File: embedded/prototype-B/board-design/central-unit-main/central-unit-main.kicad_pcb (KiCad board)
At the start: 2 copper layers, 0 parts

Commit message: [Central unit] PCB design
Finalized PCB design for the central unit.

Signed-off-by: Nicolae-Andrei Prodan <vasilenicolaeandrei@gmail.com>
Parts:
- added BAT1: 1043, 1043:1043, B.Cu at (142.0, 53.4)
- added C1: 100nF/6.3V/20%/C0603, Capacitor_SMD:C_0603_1608Metric_Pad1.08x0.95mm_HandSolder, F.Cu at (141.0, 105.0)
- added C10: 10pF/6.3V/20%/C0603, Capacitor_SMD:C_0603_1608Metric_Pad1.08x0.95mm_HandSolder, F.Cu at (159.0, 87.5)
- added C11: 22nF/6.3V/20%/C0603, Capacitor_SMD:C_0603_1608Metric_Pad1.08x0.95mm_HandSolder, F.Cu at (141.0, 103.0)
- added C12: 100nF/6.3V/20%/C0603, Capacitor_SMD:C_0603_1608Metric_Pad1.08x0.95mm_HandSolder, F.Cu at (147.2, 90.0)
- added C13: 100nF/6.3V/20%/C0603, Capacitor_SMD:C_0603_1608Metric_Pad1.08x0.95mm_HandSolder, F.Cu at (134.0, 95.0)
- added C14: 100nF/6.3V/20%/C0603, Capacitor_SMD:C_0603_1608Metric_Pad1.08x0.95mm_HandSolder, F.Cu at (134.0, 97.0)
- added C15: 100nF/6.3V/20%/C0603, Capacitor_SMD:C_0603_1608Metric_Pad1.08x0.95mm_HandSolder, F.Cu at (131.5, 102.0)
- added C16: 100nF/6.3V/20%/C0603, Capacitor_SMD:C_0603_1608Metric_Pad1.08x0.95mm_HandSolder, F.Cu at (133.5, 102.0)
- added C17: 2.2pF/6.3V/20%/C0603, Capacitor_SMD:C_0603_1608Metric_Pad1.08x0.95mm_HandSolder, F.Cu at (136.0, 79.5)
- added C18: 22uF/6.3V/20%/C0603, Capacitor_SMD:C_0603_1608Metric_Pad1.08x0.95mm_HandSolder, F.Cu at (142.0, 79.5)
- added C19: 10uF/6.3V/20%/C0603, Capacitor_SMD:C_0603_1608Metric_Pad1.08x0.95mm_HandSolder, F.Cu at (140.0, 79.5)
- added C2: 1uF/6.3V/20%/C0603, Capacitor_SMD:C_0603_1608Metric_Pad1.08x0.95mm_HandSolder, F.Cu at (141.0, 107.0)
- added C20: 100nF/6.3V/20%/C0603, Capacitor_SMD:C_0603_1608Metric_Pad1.08x0.95mm_HandSolder, F.Cu at (145.0, 80.5)
- added C21: 10uF/6.3V/20%/C0603, Capacitor_SMD:C_0603_1608Metric_Pad1.08x0.95mm_HandSolder, F.Cu at (138.0, 72.5)
- added C22: 100nF/6.3V/20%/C0603, Capacitor_SMD:C_0603_1608Metric_Pad1.08x0.95mm_HandSolder, F.Cu at (134.0, 76.5)
- added C23: 10uF/6.3V/20%/C0603, Capacitor_SMD:C_0603_1608Metric_Pad1.08x0.95mm_HandSolder, F.Cu at (145.5, 67.0)
- added C24: 10uF/6.3V/20%/C0603, Capacitor_SMD:C_0603_1608Metric_Pad1.08x0.95mm_HandSolder, F.Cu at (142.0, 62.0)
- added C25: 10uF/6.3V/20%/C0603, Capacitor_SMD:C_0603_1608Metric_Pad1.08x0.95mm_HandSolder, F.Cu at (138.0, 53.5)
- added C26: 10uF/6.3V/20%/C0603, Capacitor_SMD:C_0603_1608Metric_Pad1.08x0.95mm_HandSolder, F.Cu at (137.0, 63.0)
- added C27: 100nF/6.3V/20%/C0603, Capacitor_SMD:C_0603_1608Metric_Pad1.08x0.95mm_HandSolder, F.Cu at (145.0, 116.5)
- added C28: 10uF/6.3V/20%/C0603, Capacitor_SMD:C_0603_1608Metric_Pad1.08x0.95mm_HandSolder, F.Cu at (147.0, 116.5)
- added C29: 100nF/6.3V/20%/C0603, Capacitor_SMD:C_0603_1608Metric_Pad1.08x0.95mm_HandSolder, F.Cu at (146.0, 119.5)
- added C3: 1uF/6.3V/20%/C0603, Capacitor_SMD:C_0603_1608Metric_Pad1.08x0.95mm_HandSolder, F.Cu at (141.0, 93.0)
- added C30: 100nF/6.3V/20%/C0603, Capacitor_SMD:C_0603_1608Metric_Pad1.08x0.95mm_HandSolder, F.Cu at (146.0, 121.5)
- added C31: 10uF/6.3V/20%/C0603, Capacitor_SMD:C_0603_1608Metric_Pad1.08x0.95mm_HandSolder, F.Cu at (146.0, 123.5)
- added C32: 10uF/6.3V/20%/C0603, Capacitor_SMD:C_0603_1608Metric_Pad1.08x0.95mm_HandSolder, F.Cu at (125.0, 94.0)
- added C4: 10uF/6.3V/20%/C0603, Capacitor_SMD:C_0603_1608Metric_Pad1.08x0.95mm_HandSolder, F.Cu at (141.0, 89.0)
- added C5: 100nF/6.3V/20%/C0603, Capacitor_SMD:C_0603_1608Metric_Pad1.08x0.95mm_HandSolder, F.Cu at (147.5, 109.0)
- added C6: 100nF/6.3V/20%/C0603, Capacitor_SMD:C_0603_1608Metric_Pad1.08x0.95mm_HandSolder, F.Cu at (154.0, 109.0)
- added C7: 100nF/6.3V/20%/C0603, Capacitor_SMD:C_0603_1608Metric_Pad1.08x0.95mm_HandSolder, F.Cu at (141.0, 91.0)
- added C8: 100nF/6.3V/20%/C0603, Capacitor_SMD:C_0603_1608Metric_Pad1.08x0.95mm_HandSolder, F.Cu at (159.0, 96.0)
- added C9: 1uF/6.3V/20%/C0603, Capacitor_SMD:C_0603_1608Metric_Pad1.08x0.95mm_HandSolder, F.Cu at (159.0, 94.0)
- added D1: ESDA7P60-1U1M, ESDA7P60-1U1M:TVS_ESDA7P60-1U1M, F.Cu at (145.5, 65.0)
- added D3: LED, LED_SMD:LED_0805_2012Metric_Pad1.15x1.40mm_HandSolder, F.Cu at (135.0, 63.0)
- added D4: LED, LED_SMD:LED_0805_2012Metric_Pad1.15x1.40mm_HandSolder, F.Cu at (132.5, 63.0)
- added FB3: BLM18PG121SN1D, Inductor_SMD:L_0603_1608Metric_Pad1.05x0.95mm_HandSolder, F.Cu at (146.0, 125.5)
- added FB4: BLM18PG121SN1D, Inductor_SMD:L_0603_1608Metric_Pad1.05x0.95mm_HandSolder, F.Cu at (141.0, 109.0)
- added H1: MountingHole_Pad, MountingHole:MountingHole_4.3mm_M4_ISO7380_Pad, F.Cu at (125.0, 54.0)
- added H2: MountingHole_Pad, MountingHole:MountingHole_4.3mm_M4_ISO7380_Pad, F.Cu at (159.0, 54.0)
- added H3: MountingHole_Pad, MountingHole:MountingHole_4.3mm_M4_ISO7380_Pad, F.Cu at (159.0, 135.5)
- added H4: MountingHole_Pad, MountingHole:MountingHole_4.3mm_M4_ISO7380_Pad, F.Cu at (125.0, 135.5)
- added IC2: VEML6030, VEML6030:VEML6030, F.Cu at (142.0, 116.5)
- added IC3: STM1061N27WX6F, STM1061N27WX6F:SOT103P237X112-3N, F.Cu at (145.0, 75.5)
- added J1: Screw_Terminal_01x02, TerminalBlock_Phoenix:TerminalBlock_Phoenix_MPT-0,5-2-2.54_1x02_P2.54mm_Horizontal, B.Cu at (157.5, 80.0)
- added J2: 2171790001, 2171790001:MOLEX_2171790001, F.Cu at (160.5, 68.0)
- added J3: Conn_02x05_Odd_Even, Connector_IDC:IDC-Header_2x05_P2.54mm_Vertical, B.Cu at (147.1, 135.8)
- added J4: Conn_02x05_Odd_Even, Connector_IDC:IDC-Header_2x05_P2.54mm_Vertical, B.Cu at (158.0, 123.5)
- added J5: Conn_ARM_JTAG_SWD_20, Connector_IDC:IDC-Header_2x10_P2.54mm_Vertical, B.Cu at (126.0, 100.6)
- added L1: 2.2uH(MAMK2520T2R2M), Inductor_SMD:L_1008_2520Metric_Pad1.43x2.20mm_HandSolder, F.Cu at (141.5, 75.5)
- added R1: 0R/R0603, Resistor_SMD:R_0603_1608Metric_Pad0.98x0.95mm_HandSolder, F.Cu at (137.5, 99.0)
- added R10: 1M/R0603, Resistor_SMD:R_0603_1608Metric_Pad0.98x0.95mm_HandSolder, F.Cu at (134.0, 79.5)
- added R11: 178K/R0603, Resistor_SMD:R_0603_1608Metric_Pad0.98x0.95mm_HandSolder, F.Cu at (132.0, 79.5)
- added R12: 33K/R0603, Resistor_SMD:R_0603_1608Metric_Pad0.98x0.95mm_HandSolder, F.Cu at (145.5, 69.0)
- added R13: 5.1K/R0603, Resistor_SMD:R_0603_1608Metric_Pad0.98x0.95mm_HandSolder, F.Cu at (153.5, 69.5)
- added R14: 5.1K/R0603, Resistor_SMD:R_0603_1608Metric_Pad0.98x0.95mm_HandSolder, F.Cu at (153.5, 66.5)
- added R15: 82K/R0603, Resistor_SMD:R_0603_1608Metric_Pad0.98x0.95mm_HandSolder, F.Cu at (145.5, 71.0)
- added R16: 4.12K/R0603, Resistor_SMD:R_0603_1608Metric_Pad0.98x0.95mm_HandSolder, F.Cu at (142.0, 58.0)
- added R17: 46.4K/R0603, Resistor_SMD:R_0603_1608Metric_Pad0.98x0.95mm_HandSolder, F.Cu at (142.0, 60.0)
- added R18: 1.18K/R0603, Resistor_SMD:R_0603_1608Metric_Pad0.98x0.95mm_HandSolder, F.Cu at (139.0, 63.0)
- added R19: 1.13K/R0603, Resistor_SMD:R_0603_1608Metric_Pad0.98x0.95mm_HandSolder, F.Cu at (142.0, 56.0)
- added R2: 0R/R0603, Resistor_SMD:R_0603_1608Metric_Pad0.98x0.95mm_HandSolder, F.Cu at (137.5, 101.0)
- added R20: 1.5K/R0603, Resistor_SMD:R_0603_1608Metric_Pad0.98x0.95mm_HandSolder, F.Cu at (135.0, 67.0)
- added R21: 1.5K/R0603, Resistor_SMD:R_0603_1608Metric_Pad0.98x0.95mm_HandSolder, F.Cu at (132.5, 67.0)
- added R22: 10K/R0603, Resistor_SMD:R_0603_1608Metric_Pad0.98x0.95mm_HandSolder, F.Cu at (139.0, 116.5)
- added R23: 10K/R0603, Resistor_SMD:R_0603_1608Metric_Pad0.98x0.95mm_HandSolder, F.Cu at (139.0, 121.0)
- added R24: 10K/R0603, Resistor_SMD:R_0603_1608Metric_Pad0.98x0.95mm_HandSolder, F.Cu at (149.2, 90.0)
- added R25: 10K/R0603, Resistor_SMD:R_0603_1608Metric_Pad0.98x0.95mm_HandSolder, F.Cu at (151.2, 90.0)
- added R26: 10K/R0603, Resistor_SMD:R_0603_1608Metric_Pad0.98x0.95mm_HandSolder, F.Cu at (125.0, 92.0)
- added R27: 10K/R0603, Resistor_SMD:R_0603_1608Metric_Pad0.98x0.95mm_HandSolder, F.Cu at (132.5, 112.0)
- added R28: 10K/R0603, Resistor_SMD:R_0603_1608Metric_Pad0.98x0.95mm_HandSolder, F.Cu at (124.9, 88.0)
- added R29: 10K/R0603, Resistor_SMD:R_0603_1608Metric_Pad0.98x0.95mm_HandSolder, F.Cu at (125.0, 90.0)
- added R3: 0R/R0603, Resistor_SMD:R_0603_1608Metric_Pad0.98x0.95mm_HandSolder, F.Cu at (159.0, 100.0)
- added R30: 10K/R0603, Resistor_SMD:R_0603_1608Metric_Pad0.98x0.95mm_HandSolder, F.Cu at (125.0, 86.0)
- added R4: 1K/R0603, Resistor_SMD:R_0603_1608Metric_Pad0.98x0.95mm_HandSolder, F.Cu at (159.0, 89.5)
- added R5: 10K/R0603, Resistor_SMD:R_0603_1608Metric_Pad0.98x0.95mm_HandSolder, F.Cu at (145.2, 90.0)
- added R6: 0R/R0603, Resistor_SMD:R_0603_1608Metric_Pad0.98x0.95mm_HandSolder, F.Cu at (137.5, 95.0)
- added R7: 0R/R0603, Resistor_SMD:R_0603_1608Metric_Pad0.98x0.95mm_HandSolder, F.Cu at (137.5, 97.0)
- added R8: 100R/R0603, Resistor_SMD:R_0603_1608Metric_Pad0.98x0.95mm_HandSolder, F.Cu at (145.0, 78.5)
- added R9: 100R/R0603, Resistor_SMD:R_0603_1608Metric_Pad0.98x0.95mm_HandSolder, F.Cu at (134.0, 74.5)
- added S2: 1825910-6, 1825910-6:18259106, B.Cu at (162.0, 86.5)
- added SW1: CAS-120TA1, Button_Switch_SMD:Nidec_Copal_CAS-120A, F.Cu at (134.0, 90.0)
- added TH1: 10K/TH0603, Resistor_SMD:R_0603_1608Metric_Pad0.98x0.95mm_HandSolder, F.Cu at (149.0, 56.0)
- added TP1: TestPoint, TestPoint:TestPoint_THTPad_D2.0mm_Drill1.0mm, F.Cu at (161.2, 102.5)
- added TP2: TestPoint, TestPoint:TestPoint_THTPad_D2.0mm_Drill1.0mm, F.Cu at (129.0, 92.0)
- added TP3: TestPoint, TestPoint:TestPoint_THTPad_D2.0mm_Drill1.0mm, F.Cu at (129.0, 83.0)
- added TP4: TestPoint, TestPoint:TestPoint_THTPad_D2.0mm_Drill1.0mm, F.Cu at (159.0, 75.0)
- added TP5: TestPoint, TestPoint:TestPoint_THTPad_D2.0mm_Drill1.0mm, F.Cu at (159.0, 61.0)
- added TP6: TestPoint, TestPoint:TestPoint_THTPad_D2.0mm_Drill1.0mm, F.Cu at (155.5, 61.0)
- added TP7: TestPoint, TestPoint:TestPoint_THTPad_D2.0mm_Drill1.0mm, F.Cu at (155.5, 75.0)
- added TP8: TestPoint, TestPoint:TestPoint_THTPad_D2.0mm_Drill1.0mm, F.Cu at (129.0, 67.0)
- added U1: STM32L452RETx, Package_QFP:LQFP-64_10x10mm_P0.5mm, F.Cu at (150.0, 100.0)
- added U2: TPS63000, Package_SON:Texas_DRC0010J_ThermalVias, F.Cu at (138.0, 75.5)
- added U3: BQ24074RGT, Package_DFN_QFN:VQFN-16-1EP_3x3mm_P0.5mm_EP1.6x1.6mm, F.Cu at (138.0, 59.0)
- added U4: USBLC6-2SC6, Package_TO_SOT_SMD:SOT-23-6, F.Cu at (149.5, 68.0)
- added U5: LIS2HH12, Package_LGA:LGA-12_2x2mm_P0.5mm, F.Cu at (142.0, 121.0)
- added Y1: ECS-_327-12_5-34B-TR, Crystal:Crystal_SMD_3215-2Pin_3.2x1.5mm, F.Cu at (131.0, 96.0)
- added Y2: STDCSU1-8M, Crystal:Crystal_SMD_TXC_7A-2Pin_5x3.2mm, F.Cu at (132.5, 106.0)
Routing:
- net +3V3: track 0.00 -> 309.1 mm, vias 0 -> 5
- net /Connector/NRST: track 0.00 -> 77.8 mm, vias 0 -> 2
- net /Connector/JTDO/TRACESWO: track 0.00 -> 75.7 mm, vias 0 -> 1
- net /Connector/JTCK/SWCLK: track 0.00 -> 72.1 mm, vias 0 -> 2
- net /Connector/JTMS/SWDIO: track 0.00 -> 71.1 mm, vias 0 -> 1
- net /Connector/SPI_MOSI: track 0.00 -> 68.7 mm, vias 0 -> 1
- net /Connector/SPI_MISO: track 0.00 -> 67.9 mm, vias 0 -> 1
- net /Connector/SPI_SCK: track 0.00 -> 67.1 mm, vias 0 -> 1
- net /MCU/USB_D+: track 0.00 -> 65.5 mm, vias 0 -> 1
- net /MCU/USB_D-: track 0.00 -> 65.4 mm, vias 0 -> 1
- net /Connector/JTDI: track 0.00 -> 59.8 mm, vias 0 -> 1
- net /Connector/SPI_SS: track 0.00 -> 58.4 mm, vias 0 -> 1
- net /Connector/~{JTRST}: track 0.00 -> 54.5 mm, vias 0 -> 1
- net +BATT: track 0.00 -> 53.9 mm, vias 0 -> 2
- net /MCU/USB_DETECT: track 0.00 -> 52.0 mm
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- added copper zone on B.Cu, net GND
- added copper zone on F.Cu, net GND
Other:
- board outline added: 45 x 92.5 mm

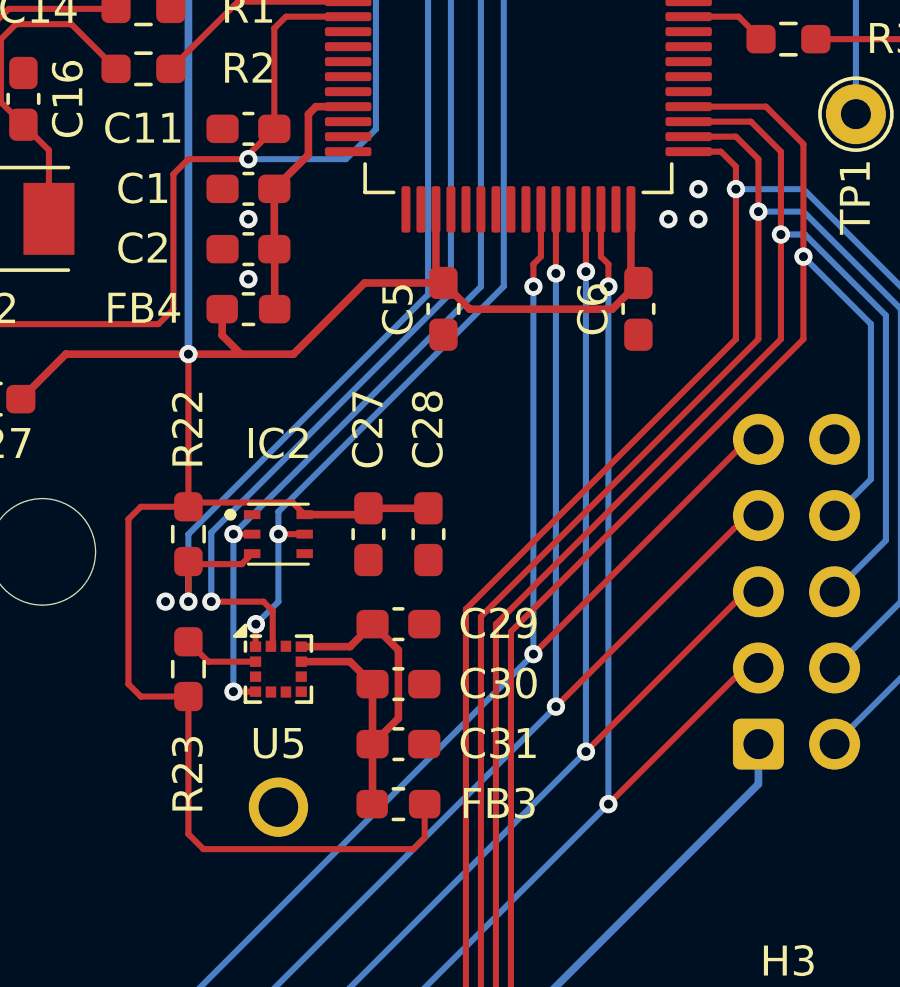
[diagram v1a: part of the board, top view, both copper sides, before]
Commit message: [All] PCB design review
Added an additional pair of pull-up resistors to the I2C signals routed
to the connectors. The PCB design looks good. Few DRC errors due to the
symbol footprints (no design error, all is within parameters). BOM,
Gerber and Drill files generated.

Signed-off-by: Nicolae-Andrei Prodan <vasilenicolaeandrei@gmail.com>
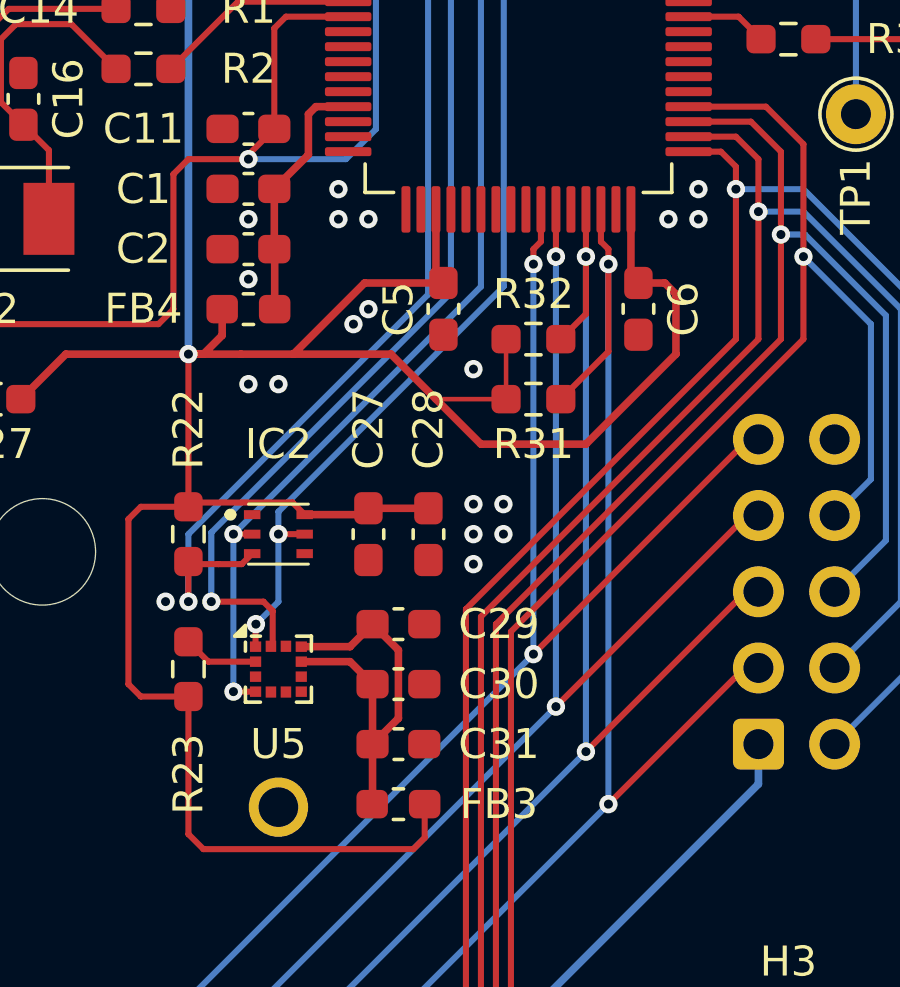
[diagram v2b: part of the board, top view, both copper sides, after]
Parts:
- added R31: 10K/R0603, Resistor_SMD:R_0603_1608Metric_Pad0.98x0.95mm_HandSolder, F.Cu at (150.5, 112.0)
- added R32: 10K/R0603, Resistor_SMD:R_0603_1608Metric_Pad0.98x0.95mm_HandSolder, F.Cu at (150.5, 110.0)
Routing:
- net +3V3: track 309.1 -> 325.4 mm
- net /Connector/I2C_SDA: track 40.6 -> 45.7 mm
- net /Connector/I2C_SCL: track 42.3 -> 45.4 mm
- net GND: vias 63 -> 76
